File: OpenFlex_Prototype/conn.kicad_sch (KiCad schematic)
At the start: 2 parts, among them J1 Molex MAX150_2x10, J2 Debug_pin_DupontConnector

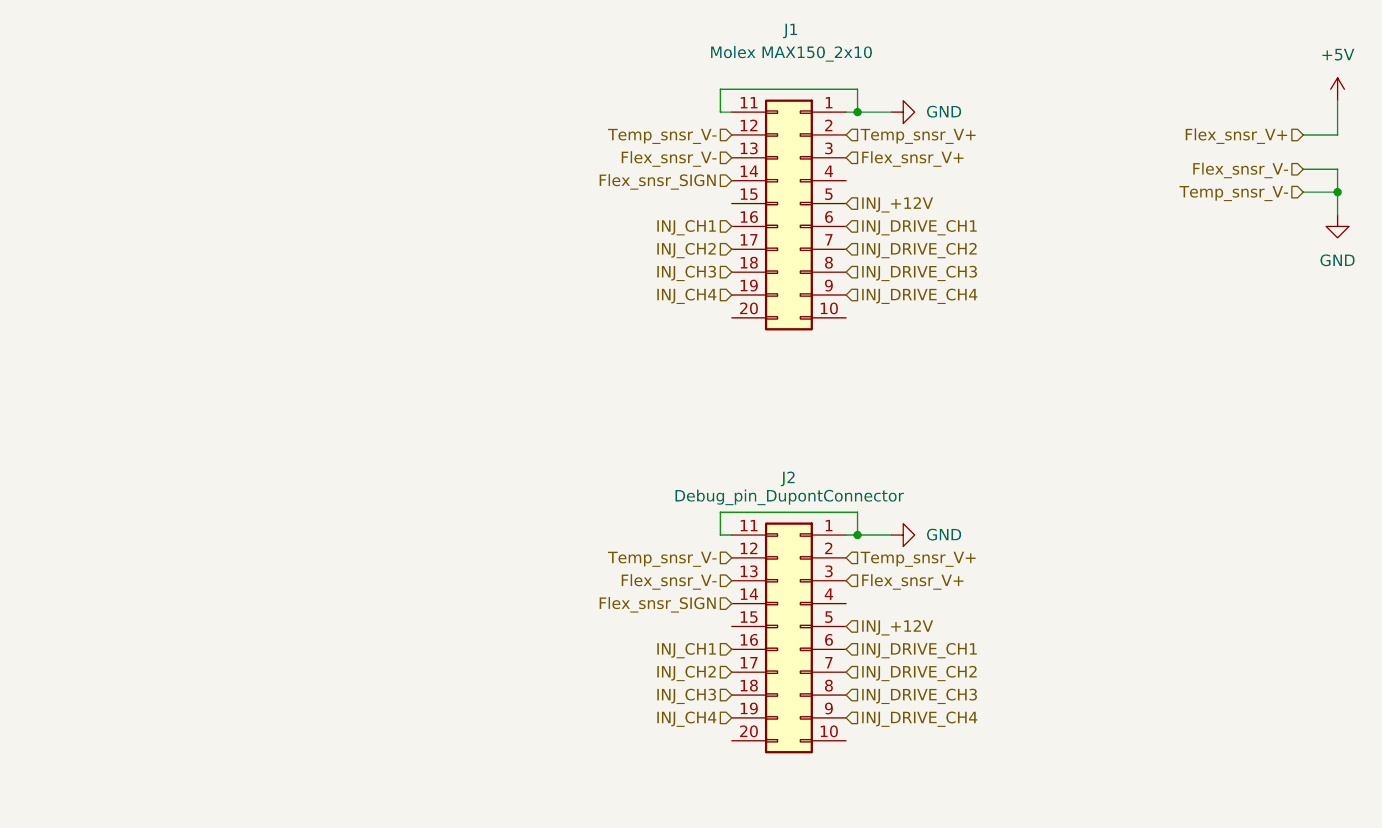
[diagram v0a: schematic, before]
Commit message: Updated PCB to ESP32-S2-Devkit-C1
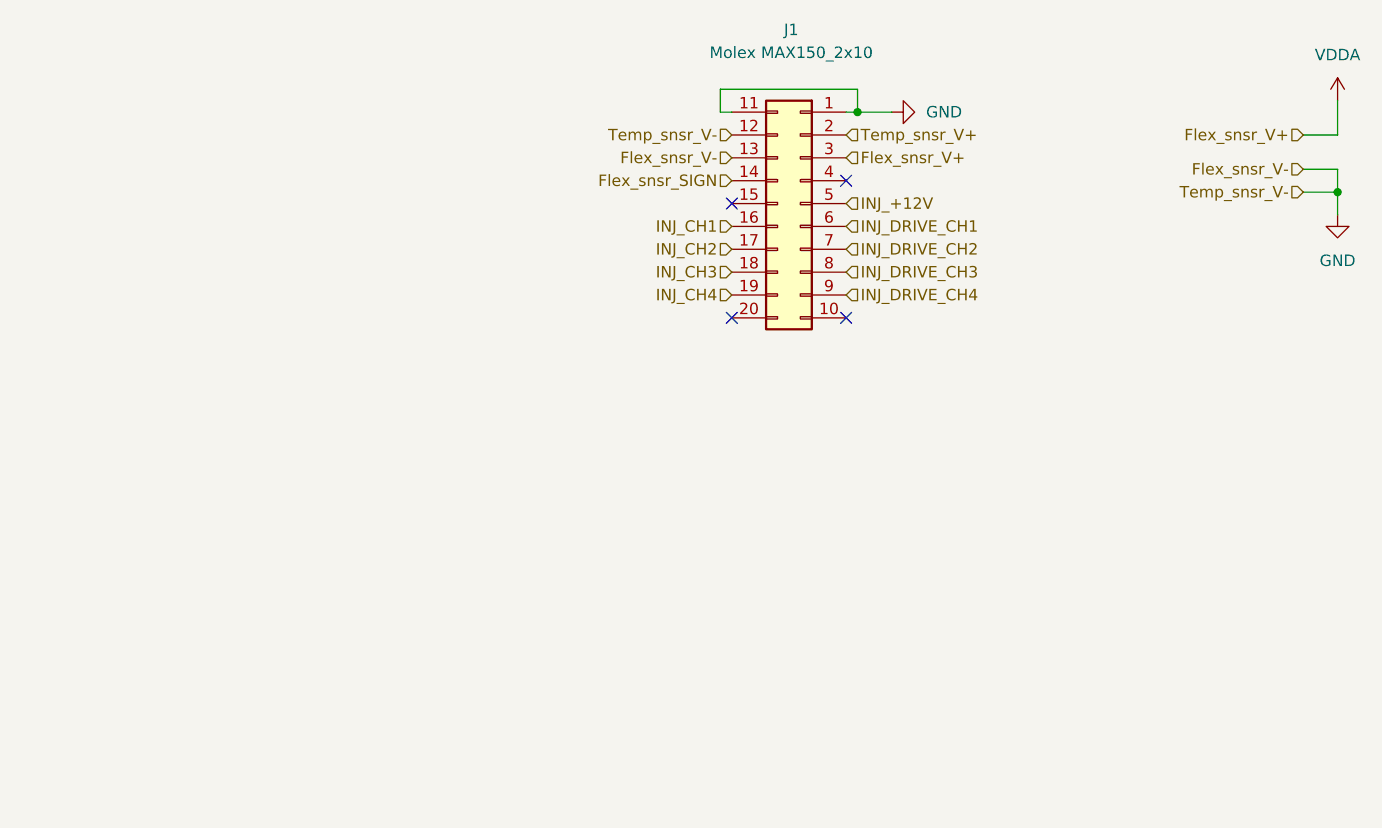
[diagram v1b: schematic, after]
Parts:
- removed J2: Debug_pin_DupontConnector, Connector_PinHeader_2.54mm:PinHeader_2x10_P2.54mm_Vertical, symbol Connector_Generic:Conn_02x10_Top_Bottom
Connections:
- net +5V renamed VDDA
- no-connect marks 0 -> 4

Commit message: Updated Sourcing for prototype
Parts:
- added J1: Molex MAX150_2x10, Open_Flex_KiCadLibrary:Molex_CONN_MX150_20w, symbol Connector_Generic:Conn_02x10_Top_Bottom
- J2: renamed from J1; Manufacturer_Part_Mating 33472-2001 -> (none); Mouser_Part_Mating 538-33472-2001 -> (none); URL_Mating https://www.mouser.fr/ProductDetail/Molex/33472-2001?qs=ZlM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 -> (none)
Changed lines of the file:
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@@
+	)
+	(symbol
+		(lib_id "Connector_Generic:Conn_02x10_Top_Bottom")
+		(at 44.45 74.93 0)
+		(mirror y)
+		(unit 1)
+		(body_style 1)
+		(exclude_from_sim no)
+		(in_bom yes)
+		(on_board no)
+		(in_pos_files yes)
+		(dnp no)
+		(property "Reference" "J1"
+			(at 43.434 55.626 0)
+			(show_name no)
+			(do_not_autoplace no)
+			(effects
+				(font
+					(size 1.27 1.27)
+				)
+			)
+		)
+		(property "Value" "Molex MAX150_2x10"
+			(at 43.434 58.166 0)
+			(show_name no)
+			(do_not_autoplace no)
+			(effects
+				(font
+					(size 1.27 1.27)
+				)
+			)
+		)
+		(property "Footprint" "Open_Flex_KiCadLibrary:Molex_CONN_MX150_20w"
+			(at 44.45 74.93 0)
+			(hide yes)
+			(show_name no)
+			(do_not_autoplace no)
+			(effects
+				(font
+					(size 1.27 1.27)
+				)
+			)
+		)
+		(property "Datasheet" ""
+			(at 44.45 74.93 0)
+			(hide yes)
+			(show_name no)
+			(do_not_autoplace no)
+			(effects
+				(font
+					(size 1.27 1.27)
+				)
+			)
+		)
+		(property "Description" "Generic connector, double row, 02x10, top/bottom pin numbering scheme (row 1: 1...pins_per_row, row2: pins_per_row+1 ... num_pins), script generated (kicad-library-utils/schlib/autogen/connector/)"
+			(at 44.45 74.93 0)
+			(hide yes)
+			(show_name no)
+			(do_not_autoplace no)
+			(effects
+				(font
+					(size 1.27 1.27)
+				)
+			)
+		)
+		(property "Manufacturer_Name" "Molex"
+			(at 44.45 74.93 0)
+			(hide yes)
+			(show_name no)
+			(do_not_autoplace no)
+			(effects
+				(font
+					(size 1.27 1.27)
+				)
+			)
+		)
+		(property "Manufacturer_Part_Number" "Manufacturer_Part_Mating 33472-2001  0 0 Centrer Centrer 0 0 "
+			(at 44.45 74.93 0)
+			(hide yes)
+			(show_name no)
+			(do_not_autoplace no)
+			(effects
+				(font
+					(size 1.27 1.27)
+				)
+			)
+		)
+		(property "Mouser_Part_Number" "538-33472-2001 "
+			(at 44.45 74.93 0)
+			(hide yes)
+			(show_name no)
+			(do_not_autoplace no)
+			(effects
+				(font
+					(size 1.27 1.27)
+				)
+			)
+		)
+		(property "URL" "https://www.mouser.fr/ProductDetail/Molex/33472-2001?qs=ZlMU7IUseCt4wlAgpUcMsQ%3D%3D"
+			(at 44.45 74.93 0)
+			(hide yes)
+			(show_name no)
+			(do_not_autoplace no)
+			(effects
+				(font
+					(size 1.27 1.27)
+				)
+			)
+		)
+		(pin "1"
+		)
+		(pin "10"
+		)
+		(pin "15"
+		)
+		(pin "17"
+		)
+		(pin "18"
+		)
+		(pin "19"
+		)
+		(pin "2"
+		)
+		(pin "3"
+		)
+		(pin "9"
+		)
+		(pin "5"
+		)
+		(pin "6"
+		)
+		(pin "7"
+		)
+		(pin "8"
+		)
+		(pin "11"
+		)
+		(pin "13"
+		)
+		(pin "14"
+		)
+		(pin "16"
+		)
+		(pin "4"
+		)
+		(pin "12"
+		)
+		(pin "20"
+		)
+		(instances
+			(project "Open_FlexFuel_Nano_THT"
+				(path "/9b5751a0-d284-4a5b-96bd-00759eb74951/b70e50ac-d40c-421a-87c6-6289c5083853"
+					(reference "J1")
+					(unit 1)
+				)
+			)
+		)
 	)
 	(symbol
@@
 		(in_pos_files yes)
 		(dnp no)
-		(property "Reference" "J1"
+		(property "Reference" "J2"
 			(at 100.584 55.626 0)
 			(show_name no)
@@
 		)
 		(property "URL" "https://www.mouser.fr/ProductDetail/Molex/34830-2001?qs=PdnAIJ6Mlf3cw4zbnnbtng%3D%3D"
-			(at 101.6 74.93 0)
-			(hide yes)
-			(show_name no)
-			(do_not_autoplace no)
-			(effects
-				(font
-					(size 1.27 1.27)
-				)
-			)
-		)
-		(property "Manufacturer_Part_Mating" "33472-2001 "
-			(at 101.6 74.93 0)
-			(hide yes)
-			(show_name no)
-			(do_not_autoplace no)
-			(effects
-				(font
-					(size 1.27 1.27)
-				)
-			)
-		)
-		(property "Mouser_Part_Mating" "538-33472-2001 "
-			(at 101.6 74.93 0)
-			(hide yes)
-			(show_name no)
-			(do_not_autoplace no)
-			(effects
-				(font
-					(size 1.27 1.27)
-				)
-			)
-		)
-		(property "URL_Mating" "https://www.mouser.fr/ProductDetail/Molex/33472-2001?qs=ZlMU7IUseCt4wlAgpUcMsQ%3D%3D"
 			(at 101.6 74.93 0)
 			(hide yes)
@@
 			(project "Open_FlexFuel_Nano_THT"
 				(path "/9b5751a0-d284-4a5b-96bd-00759eb74951/b70e50ac-d40c-421a-87c6-6289c5083853"
-					(reference "J1")
+					(reference "J2")
 					(unit 1)
 				)

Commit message: Updated BOM
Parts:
- added J10, J11, J12, J13, J14, J15, J16, J17, J18, J19, J20, J21, J22, J3, J4, J5, J6, J7, J8, J9: Conn_01x01_Pin, symbol Connector:Conn_01x01_Pin
- J1: Manufacturer_Part_Number Manufacturer_Part_Mating 33472-2001 0 0 Centrer Centrer 0 0 -> 33472-2001
